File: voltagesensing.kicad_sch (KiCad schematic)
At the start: 0 parts

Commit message: Schematic Editing Done
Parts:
- added C1: 470nF, Capacitor_THT:C_Rect_L32.0mm_W15.0mm_P27.00mm, symbol Device:C
- added C2: 470uF, Capacitor_SMD:CP_Elec_6.3x7.7, symbol Device:C_Polarized_US
- added C3, C4: 10uF, Capacitor_SMD:C_0402_1005Metric, symbol Device:C
- added C5, C7: 10uF, symbol Device:C_Polarized_US
- added C6: 0.1uF, Capacitor_SMD:C_1206_3216Metric, symbol Device:C
- added D3: 7.5, Diode_SMD:D_MiniMELF, symbol Device:D_Zener_Filled
- added D4: 1N4007, Diode_THT:D_DO-41_SOD81_P10.16mm_Horizontal, symbol Diode:1N4007
- added R10, R9: 100K, Resistor_THT:R_Axial_DIN0207_L6.3mm_D2.5mm_P15.24mm_Horizontal, symbol Device:R
- added R11: 220K, Resistor_THT:R_Axial_DIN0207_L6.3mm_D2.5mm_P15.24mm_Horizontal, symbol Device:R
- added R12: 1K, Resistor_THT:R_Axial_DIN0207_L6.3mm_D2.5mm_P15.24mm_Horizontal, symbol Device:R
- added R5: 220, Resistor_THT:R_Axial_DIN0414_L11.9mm_D4.5mm_P15.24mm_Horizontal, symbol Device:R
- added R6: 470k, Resistor_THT:R_Axial_DIN0207_L6.3mm_D2.5mm_P15.24mm_Horizontal, symbol Device:R
- added R7, R8: 1M, Resistor_THT:R_Axial_DIN0207_L6.3mm_D2.5mm_P15.24mm_Horizontal, symbol Device:R
- added U3: AMS1117-5.0, Package_TO_SOT_SMD:SOT-223-3_TabPin2, symbol Regulator_Linear:AMS1117-5.0
- added U4: AMC1200SDUBR, DUB0008A-IPC_A, symbol 2025-08-05_00-17-59:AMC1200SDUBR
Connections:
- new net: C1.2, D3.1 (K), D4.2 (A), R6.2
- new net: C5.1, R10.1, R12.2, R9.2, U4.3 (VINN)
- new net: C2.1, C3.1, D4.1 (K), U3.3 (VI)
- new net: R11.2, R12.1, U4.2 (VINP)
- new net: C1.1, R5.2, R6.1
- new net: R11.1, R8.2
- new net: R7.2, R8.1
- new net AC sensing: U4.7 (VOUTP)
- new net GND: C7.2, U4.5 (GND2)
- new net GND1: C2.2, C3.2, C4.2, C5.2, C6.1, D3.2 (A), R10.2, U3.1 (GND), U4.4 (GND1)
- new net L: R5.1, R7.1
- new net VCC_3.3: C7.1, U4.8 (VDD2)
- new net VDD1: C4.1, C6.2, R9.1, U3.2 (VO), U4.1 (VDD1)
- no-connect marks 0 -> 1
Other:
- note added: "Cap-Drop Power Supply with voltage Regulator"

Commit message: Assignment Of Footprint Done
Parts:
- C1: footprint Capacitor_THT:C_Rect_L32.0mm_W15.0mm_P27.00mm -> capacitor:RESAD4580W75L4100D850; voltage 400V -> 630V
- C2: footprint Capacitor_SMD:CP_Elec_6.3x7.7 -> Capacitor_THT:CP_Axial_L11.0mm_D8.0mm_P15.00mm_Horizontal
- C3, C4: footprint Capacitor_SMD:C_0402_1005Metric -> Capacitor_SMD:C_1206_3216Metric_Pad1.33x1.80mm_HandSolder
- C5, C7: footprint (none) -> Capacitor_THT:CP_Axial_L11.0mm_D5.0mm_P18.00mm_Horizontal
- R10, R11, R12, R6, R7, R8, R9: footprint Resistor_THT:R_Axial_DIN0207_L6.3mm_D2.5mm_P15.24mm_Horizontal -> Resistor_THT:R_Axial_DIN0207_L6.3mm_D2.5mm_P10.16mm_Horizontal
- U4: footprint DUB0008A-IPC_A -> AMC1200SDUBR:DUB0008A-IPC_A
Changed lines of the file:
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@@
 			)
 		)
-		(property "Footprint" "Resistor_THT:R_Axial_DIN0207_L6.3mm_D2.5mm_P15.24mm_Horizontal"
+		(property "Footprint" "Resistor_THT:R_Axial_DIN0207_L6.3mm_D2.5mm_P10.16mm_Horizontal"
 			(at 134.112 107.95 90)
 			(effects
@@
 			)
 		)
-		(property "Footprint" "Capacitor_SMD:C_0402_1005Metric"
+		(property "Footprint" "Capacitor_SMD:C_1206_3216Metric_Pad1.33x1.80mm_HandSolder"
 			(at 124.1552 113.03 0)
 			(effects
@@
 			)
 		)
-		(property "Footprint" "DUB0008A-IPC_A"
+		(property "Footprint" "AMC1200SDUBR:DUB0008A-IPC_A"
 			(at 195.58 97.79 0)
 			(effects
@@
 			)
 		)
-		(property "Footprint" ""
+		(property "Footprint" "Capacitor_THT:CP_Axial_L11.0mm_D5.0mm_P18.00mm_Horizontal"
 			(at 246.38 92.71 0)
 			(effects
@@
 			)
 		)
-		(property "Footprint" "Resistor_THT:R_Axial_DIN0207_L6.3mm_D2.5mm_P15.24mm_Horizontal"
+		(property "Footprint" "Resistor_THT:R_Axial_DIN0207_L6.3mm_D2.5mm_P10.16mm_Horizontal"
 			(at 148.082 83.82 90)
 			(effects
@@
 			)
 		)
-		(property "Footprint" "Resistor_THT:R_Axial_DIN0207_L6.3mm_D2.5mm_P15.24mm_Horizontal"
+		(property "Footprint" "Resistor_THT:R_Axial_DIN0207_L6.3mm_D2.5mm_P10.16mm_Horizontal"
 			(at 134.112 118.11 90)
 			(effects
@@
 			)
 		)
-		(property "Footprint" "Resistor_THT:R_Axial_DIN0207_L6.3mm_D2.5mm_P15.24mm_Horizontal"
+		(property "Footprint" "Resistor_THT:R_Axial_DIN0207_L6.3mm_D2.5mm_P10.16mm_Horizontal"
 			(at 148.082 107.95 90)
 			(effects
@@
 			)
 		)
-		(property "Footprint" "Resistor_THT:R_Axial_DIN0207_L6.3mm_D2.5mm_P15.24mm_Horizontal"
+		(property "Footprint" "Resistor_THT:R_Axial_DIN0207_L6.3mm_D2.5mm_P10.16mm_Horizontal"
 			(at 128.27 67.818 90)
 			(effects
@@
 			)
 		)
-		(property "Footprint" "Capacitor_THT:C_Rect_L32.0mm_W15.0mm_P27.00mm"
+		(property "Footprint" "capacitor:RESAD4580W75L4100D850"
 			(at 67.31 103.1748 0)
 			(effects
@@
 			)
 		)
-		(property "voltage" "400V"
+		(property "voltage" "630V"
 			(at 63.5 99.06 90)
 			(effects
@@
 			)
 		)
-		(property "Footprint" "Resistor_THT:R_Axial_DIN0207_L6.3mm_D2.5mm_P15.24mm_Horizontal"
+		(property "Footprint" "Resistor_THT:R_Axial_DIN0207_L6.3mm_D2.5mm_P10.16mm_Horizontal"
 			(at 104.14 67.818 90)
 			(effects
@@
 			)
 		)
-		(property "Footprint" "Resistor_THT:R_Axial_DIN0207_L6.3mm_D2.5mm_P15.24mm_Horizontal"
+		(property "Footprint" "Resistor_THT:R_Axial_DIN0207_L6.3mm_D2.5mm_P10.16mm_Horizontal"
 			(at 63.5 110.998 90)
 			(effects
@@
 			)
 		)
-		(property "Footprint" "Capacitor_SMD:CP_Elec_6.3x7.7"
+		(property "Footprint" "Capacitor_THT:CP_Axial_L11.0mm_D8.0mm_P15.00mm_Horizontal"
 			(at 86.36 109.22 0)
 			(effects
@@
 			)
 		)
-		(property "Footprint" ""
+		(property "Footprint" "Capacitor_THT:CP_Axial_L11.0mm_D5.0mm_P18.00mm_Horizontal"
 			(at 149.86 116.84 0)
 			(effects
@@
 			)
 		)
-		(property "Footprint" "Capacitor_SMD:C_0402_1005Metric"
+		(property "Footprint" "Capacitor_SMD:C_1206_3216Metric_Pad1.33x1.80mm_HandSolder"
 			(at 102.5652 113.03 0)
 			(effects

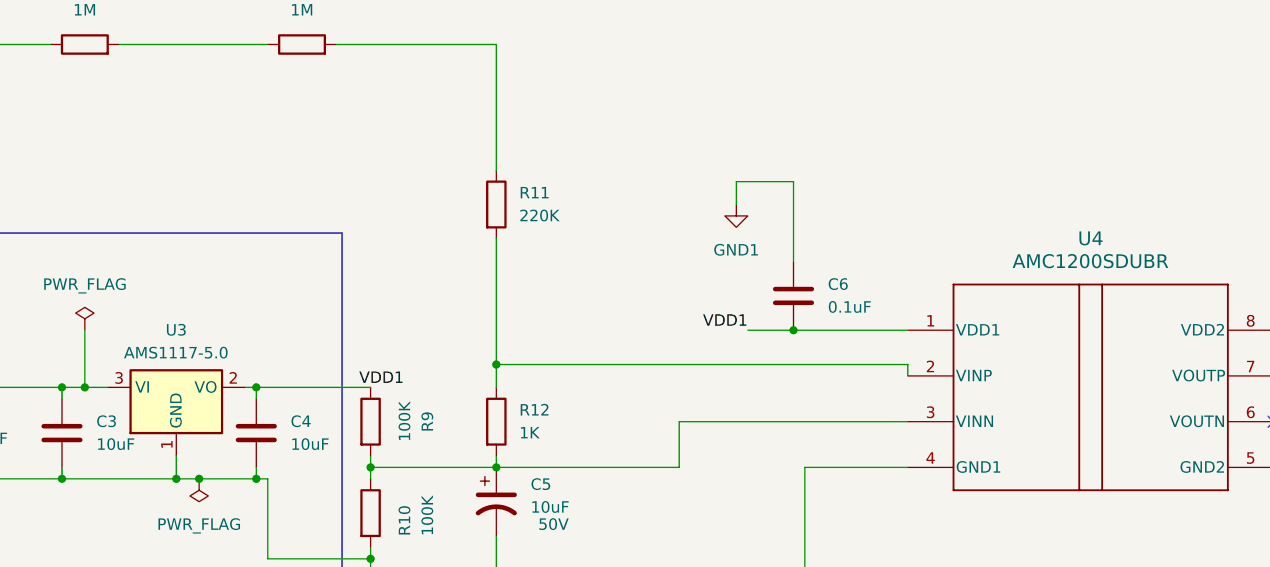
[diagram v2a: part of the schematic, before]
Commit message: Placement Of Component on PCB Done
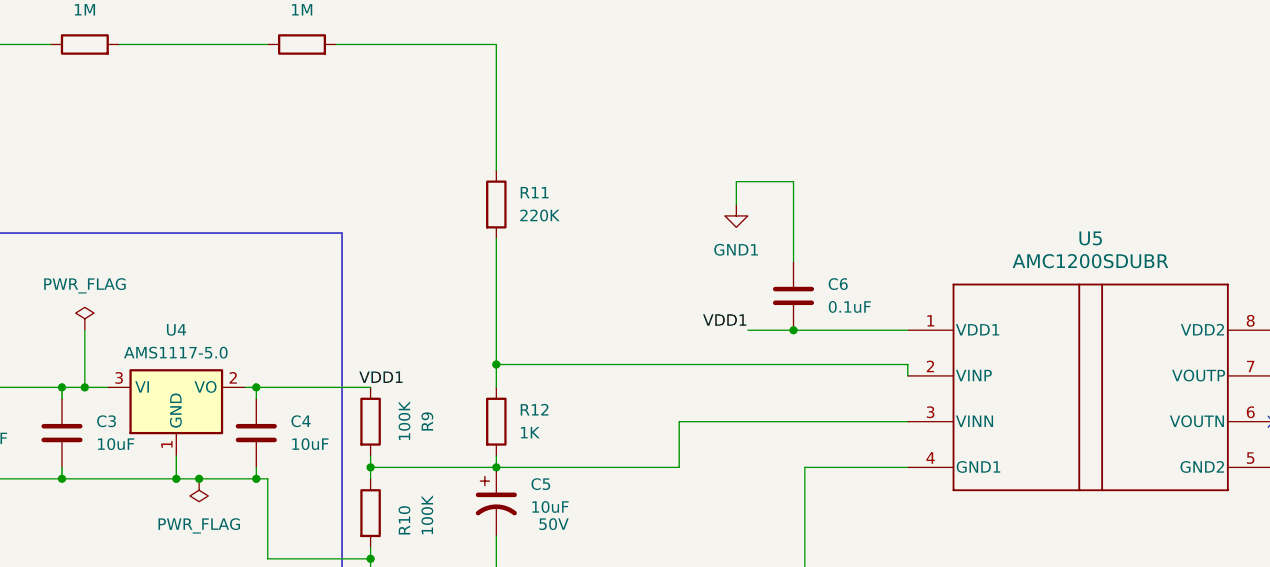
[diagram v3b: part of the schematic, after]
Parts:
- C1: footprint capacitor:RESAD4580W75L4100D850 -> capacitor:CAP_150AXIAL_RF_CND
- C2: footprint Capacitor_THT:CP_Axial_L11.0mm_D8.0mm_P15.00mm_Horizontal -> Capacitor_THT:CP_Radial_D5.0mm_P2.50mm
- C5, C7: footprint Capacitor_THT:CP_Axial_L11.0mm_D5.0mm_P18.00mm_Horizontal -> Capacitor_THT:CP_Radial_D5.0mm_P2.50mm
- renumbered U3 to U4, U4 to U5
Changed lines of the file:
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@@
+		)
+	)
+	(netclass_flag ""
+		(length 2.54)
+		(shape round)
+		(at 38.1 114.3 0)
+		(fields_autoplaced yes)
+		(effects
+			(font
+				(size 1.27 1.27)
+			)
+			(justify left bottom)
+		)
+		(property "Netclass" "AC "
+			(at 38.7985 111.76 0)
+			(effects
+				(font
+					(size 1.27 1.27)
+				)
+				(justify left)
+			)
+		)
+		(property "Component Class" ""
+			(at 0 -1.27 0)
+			(effects
+				(font
+					(size 1.27 1.27)
+					(italic yes)
+				)
+			)
 		)
 	)
@@
 		(dnp no)
 		(fields_autoplaced yes)
-		(property "Reference" "U3"
+		(property "Reference" "U4"
 			(at 114.3 97.79 0)
 			(effects
@@
 			(project "ESP_Edgedevice"
 				(path "/8fa9f2a2-260d-4024-b3c1-a0bc52ef0867/806ba1af-f0ba-4182-8795-26f4db8d47a2"
-					(reference "U3")
+					(reference "U4")
 					(unit 1)
 				)
@@
 		(dnp no)
 		(fields_autoplaced yes)
-		(property "Reference" "U4"
+		(property "Reference" "U5"
 			(at 215.9 87.63 0)
 			(effects
@@
 			(project "ESP_Edgedevice"
 				(path "/8fa9f2a2-260d-4024-b3c1-a0bc52ef0867/806ba1af-f0ba-4182-8795-26f4db8d47a2"
-					(reference "U4")
+					(reference "U5")
 					(unit 1)
 				)
@@
 			)
 		)
-		(property "Footprint" "Capacitor_THT:CP_Axial_L11.0mm_D5.0mm_P18.00mm_Horizontal"
+		(property "Footprint" "Capacitor_THT:CP_Radial_D5.0mm_P2.50mm"
 			(at 246.38 92.71 0)
 			(effects
@@
 			)
 		)
-		(property "Footprint" "capacitor:RESAD4580W75L4100D850"
+		(property "Footprint" "capacitor:CAP_150AXIAL_RF_CND"
 			(at 67.31 103.1748 0)
 			(effects
@@
 			)
 		)
-		(property "Footprint" "Capacitor_THT:CP_Axial_L11.0mm_D8.0mm_P15.00mm_Horizontal"
+		(property "Footprint" "Capacitor_THT:CP_Radial_D5.0mm_P2.50mm"
 			(at 86.36 109.22 0)
 			(effects
@@
 			)
 		)
-		(property "Footprint" "Capacitor_THT:CP_Axial_L11.0mm_D5.0mm_P18.00mm_Horizontal"
+		(property "Footprint" "Capacitor_THT:CP_Radial_D5.0mm_P2.50mm"
 			(at 149.86 116.84 0)
 			(effects

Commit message: FINAL COMMIT
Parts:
- C2: footprint Capacitor_THT:CP_Radial_D5.0mm_P2.50mm -> Capacitor_THT:CP_Radial_D10.0mm_P5.00mm
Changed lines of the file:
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@@
 			)
 		)
-		(property "Footprint" "Capacitor_THT:CP_Radial_D5.0mm_P2.50mm"
+		(property "Footprint" "Capacitor_THT:CP_Radial_D10.0mm_P5.00mm"
 			(at 86.36 109.22 0)
 			(effects
